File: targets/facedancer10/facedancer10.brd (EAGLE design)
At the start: 71.1 x 23.5 mm, 20 parts, among them CN1 HOST, CN2 VICTIM, Q1 12MHz, U1 F261X---PM64, U2 FT232RL-BASICSSOP, U3 MAX3420ELQFP32

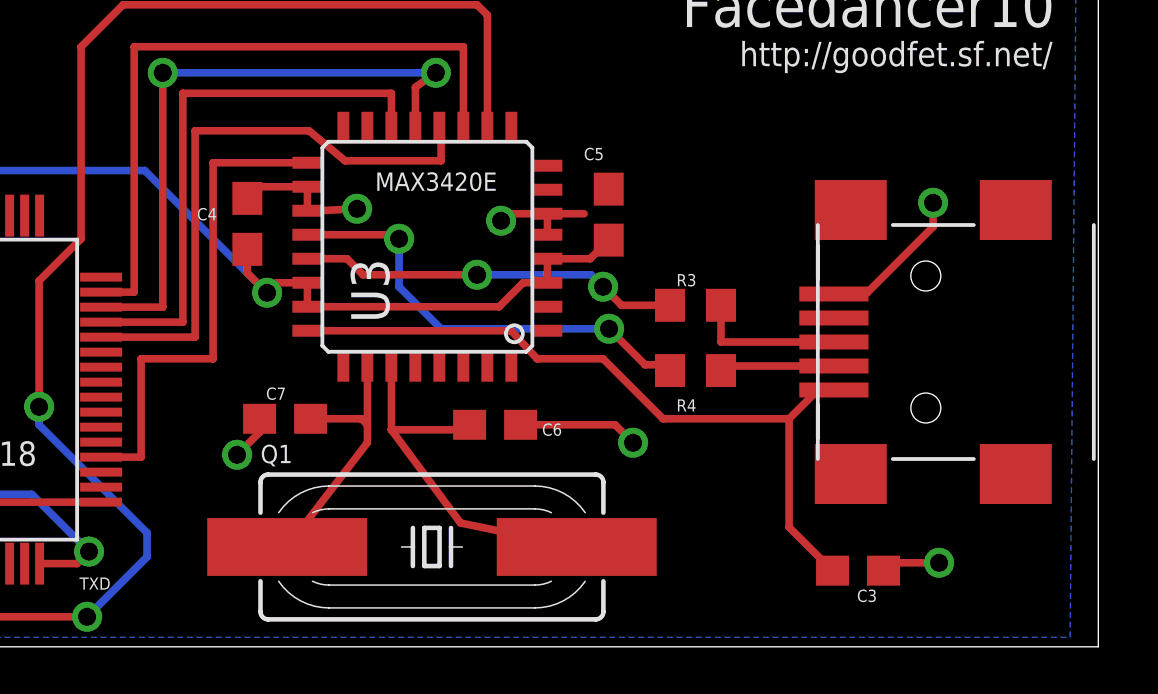
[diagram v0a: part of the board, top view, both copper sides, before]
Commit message: Fixing Facedancer layout.
git-svn-id: https://svn.code.sf.net/p/goodfet/code@1134 12e2690d-a6be-4b82-a7b7-67c4a43b65c8
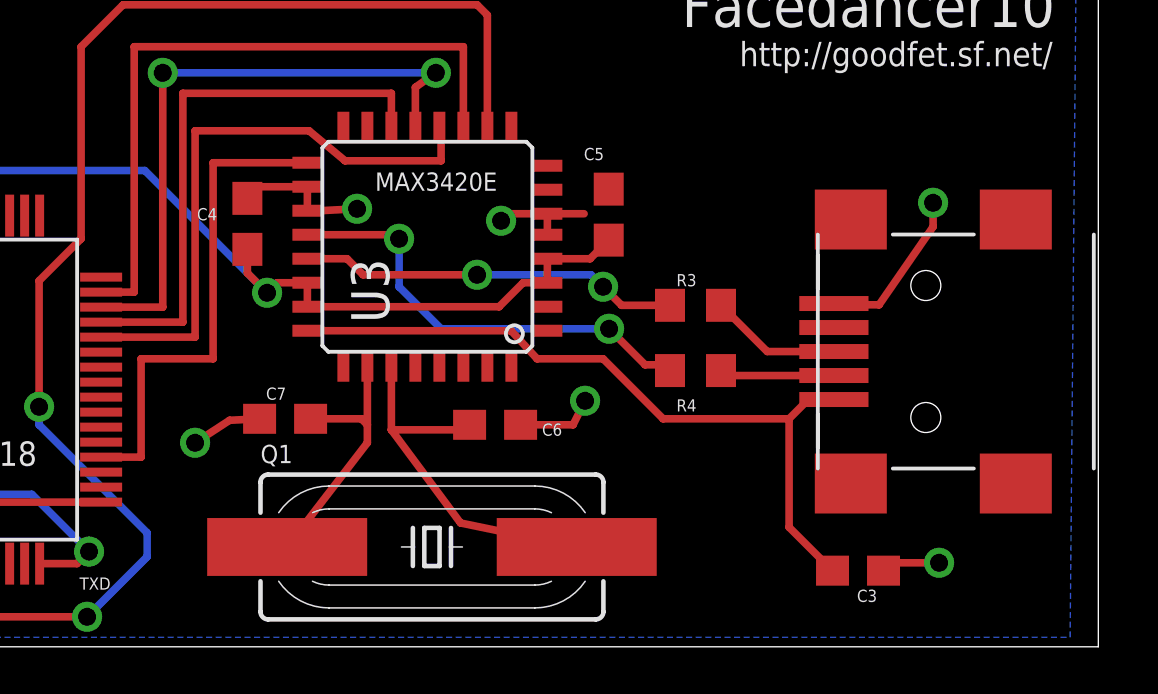
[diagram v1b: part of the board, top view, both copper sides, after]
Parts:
- moved CN2 0.32 mm to (66.4, 9.84)
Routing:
- net N$11: track 4.99 -> 4.40 mm
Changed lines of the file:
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@@
 <attribute name="VALUE" x="57.8635" y="0.18" size="1.27" layer="27" ratio="10" rot="R90"/>
 </element>
-<element name="CN2" library="adafruit" package="USB-MINIB" value="VICTIM" x="66.3575" y="10.16" smashed="yes" rot="R90">
-<attribute name="VALUE" x="62.45" y="16.0925" size="1.27" layer="27"/>
+<element name="CN2" library="adafruit" package="USB-MINIB" value="VICTIM" x="66.3575" y="9.8425" smashed="yes" rot="R90">
+<attribute name="VALUE" x="62.45" y="15.775" size="1.27" layer="27"/>
 </element>
 <element name="R3" library="rcl" package="R0603" value="33" x="57.68" y="11.3825" smashed="yes">
@@
 <via x="46.4" y="14.6" extent="1-16" drill="0.6"/>
 <via x="51.2" y="14.2" extent="1-16" drill="0.6"/>
-<wire x1="62.2935" y1="11.76" x2="62.3335" y2="11.8" width="0.254" layer="1"/>
-<wire x1="62.3335" y1="11.8" x2="63.4" y2="11.8" width="0.254" layer="1"/>
-<wire x1="63.4" y1="11.8" x2="65.6" y2="14" width="0.254" layer="1"/>
+<wire x1="62.2935" y1="11.4425" x2="62.7335" y2="11.4" width="0.254" layer="1"/>
+<wire x1="62.7335" y1="11.4" x2="63.8" y2="11.4" width="0.254" layer="1"/>
+<wire x1="63.8" y1="11.4" x2="65.6" y2="14" width="0.254" layer="1"/>
 <via x="65.6" y="14.8" extent="1-16" drill="0.6"/>
 <wire x1="63.9475" y1="2.5375" x2="64.21" y2="2.8" width="0.254" layer="1"/>
@@
 <contactref element="C7" pad="1"/>
 <contactref element="C6" pad="1"/>
-<wire x1="43.15" y1="7.6" x2="43.15" y2="7.15" width="0.254" layer="1"/>
-<wire x1="43.15" y1="7.15" x2="42.4" y2="6.4" width="0.254" layer="1"/>
-<via x="42.4" y="6.4" extent="1-16" drill="0.6"/>
-<wire x1="51.85" y1="7.4" x2="55" y2="7.4" width="0.254" layer="1"/>
-<wire x1="55" y1="7.4" x2="55.6" y2="6.8" width="0.254" layer="1"/>
-<via x="55.6" y="6.8" extent="1-16" drill="0.6"/>
+<wire x1="43.15" y1="7.6" x2="42.15" y2="7.55" width="0.254" layer="1"/>
+<wire x1="42.15" y1="7.55" x2="41" y2="6.8" width="0.254" layer="1"/>
+<via x="41" y="6.8" extent="1-16" drill="0.6"/>
+<wire x1="51.85" y1="7.4" x2="53.6" y2="7.4" width="0.254" layer="1"/>
+<wire x1="53.6" y1="7.4" x2="54" y2="8.2" width="0.254" layer="1"/>
+<via x="54" y="8.2" extent="1-16" drill="0.6"/>
 <wire x1="53.9675" y1="14.435" x2="54.7875" y2="15.255" width="0" layer="19" extent="1-1"/>
 <wire x1="42.7425" y1="14.9475" x2="42.8" y2="15" width="0" layer="19" extent="1-1"/>
@@
 <wire x1="62.2475" y1="2.5375" x2="60.8" y2="3.985" width="0.254" layer="1"/>
 <wire x1="60.8" y1="3.985" x2="60.8" y2="7.6" width="0.254" layer="1"/>
-<wire x1="60.8" y1="7.6" x2="61.76" y2="8.56" width="0.254" layer="1"/>
-<wire x1="61.76" y1="8.56" x2="62.2935" y2="8.56" width="0.254" layer="1"/>
 <wire x1="60.8" y1="7.6" x2="56.6" y2="7.6" width="0.254" layer="1"/>
 <wire x1="44.7425" y1="10.535" x2="51.535" y2="10.535" width="0.254" layer="1"/>
@@
 <wire x1="52.4" y1="9.6" x2="54.6" y2="9.6" width="0.254" layer="1"/>
 <wire x1="54.6" y1="9.6" x2="56.6" y2="7.6" width="0.254" layer="1"/>
+<wire x1="62.2935" y1="8.2425" x2="61.4425" y2="8.2425" width="0.254" layer="1"/>
+<wire x1="61.4425" y1="8.2425" x2="60.8" y2="7.6" width="0.254" layer="1"/>
 </signal>
 <signal name="N$10">
 <contactref element="CN2" pad="D-"/>
 <contactref element="R4" pad="2"/>
-<wire x1="62.2935" y1="9.36" x2="58.53" y2="9.36" width="0.254" layer="1"/>
 <wire x1="58.53" y1="9.36" x2="58.53" y2="9.2075" width="0.254" layer="1"/>
+<wire x1="62.2935" y1="9.0425" x2="58.7575" y2="9.0425" width="0.254" layer="1"/>
+<wire x1="58.7575" y1="9.0425" x2="58.6" y2="9.2" width="0.254" layer="1"/>
+<wire x1="58.6" y1="9.2" x2="58.5375" y2="9.2" width="0.254" layer="1"/>
+<wire x1="58.5375" y1="9.2" x2="58.53" y2="9.2075" width="0.254" layer="1"/>
 </signal>
 <signal name="N$11">
 <contactref element="CN2" pad="D+"/>
 <contactref element="R3" pad="2"/>
-<wire x1="62.2935" y1="10.16" x2="58.53" y2="10.16" width="0.254" layer="1"/>
-<wire x1="58.53" y1="10.16" x2="58.53" y2="11.3825" width="0.254" layer="1"/>
+<wire x1="62.2935" y1="9.8425" x2="60.07" y2="9.8425" width="0.254" layer="1"/>
+<wire x1="60.07" y1="9.8425" x2="58.53" y2="11.3825" width="0.254" layer="1"/>
 </signal>
 </signals>
